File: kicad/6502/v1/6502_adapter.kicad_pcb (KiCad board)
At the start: 2 copper layers, 49 x 75.2 mm, 53 parts, among them P1 Conn_02x20_Odd_Even, P2 Conn_02x20_Odd_Even, P3 Conn_01x03, SW1 SW_Push, SW2 SW_Push, U1 WD65C02, U2 74LVC4245, U3 74LVC4245, U4 74LVC4245, U5 74LVC4245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

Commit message: Kicad 6502: final tweaks
Change-Id: Id3d45fc11b7cfa304b3275ba0561da354e969d0a
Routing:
- net /5V: track 231.6 -> 232.9 mm
- net /nML: track 35.8 -> 34.9 mm
- net /RnW: track 45.1 -> 45.6 mm
- net /GND: track 264.4 -> 264.9 mm, vias 33 -> 34
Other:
- board text added: "BkPt"
- board text added: "Optional bus enable components"
- board text removed: "BrkPt"
- board text removed: "Optional Bus Enable (BE) components"

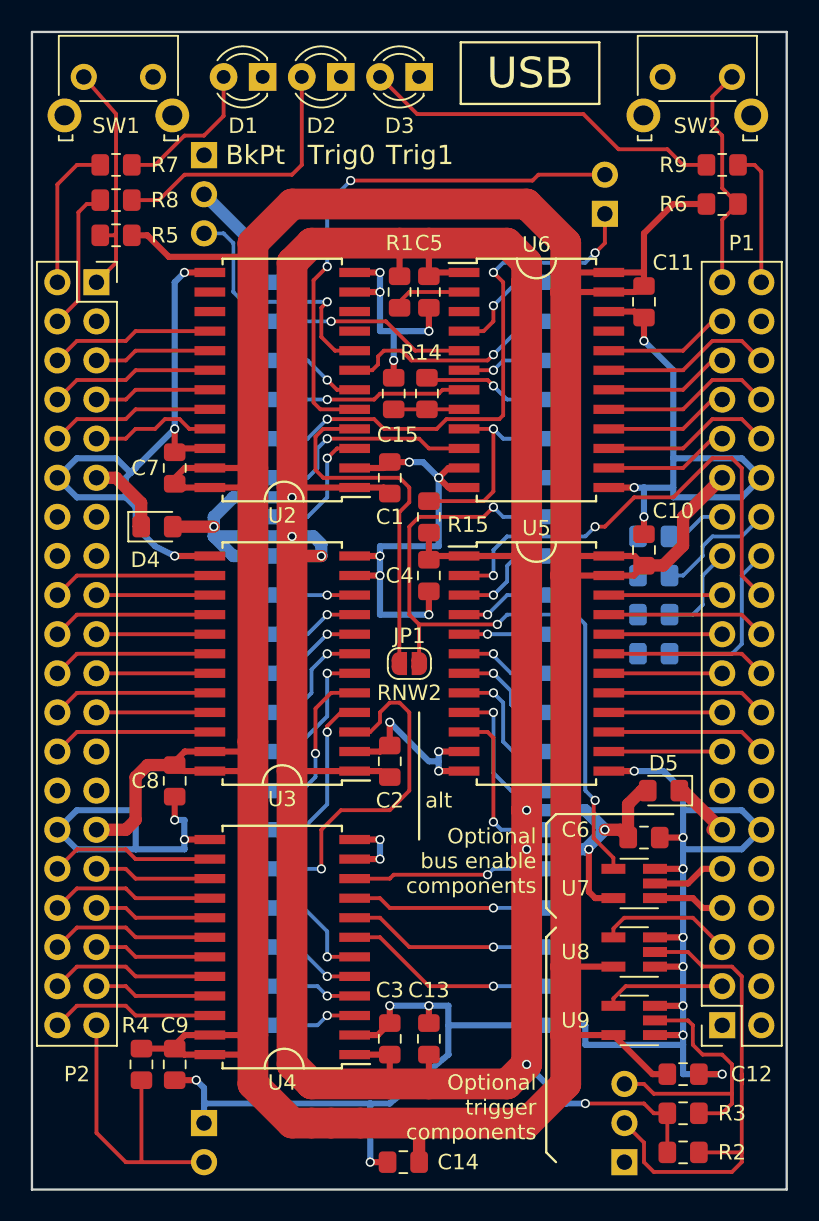
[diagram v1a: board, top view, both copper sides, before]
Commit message: Kicad 6502: add more power vias
Change-Id: I293a495840e0f96dae8bd8866a7b1adfe1f79e49
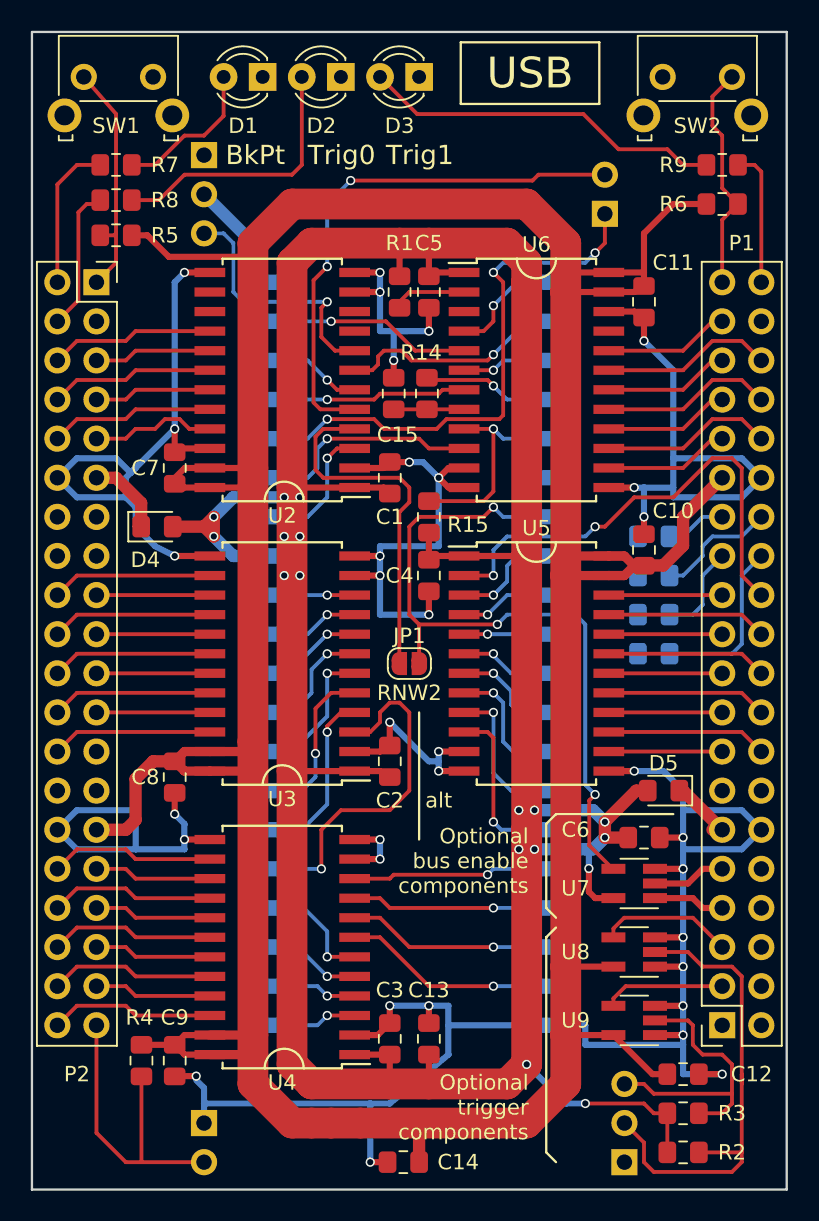
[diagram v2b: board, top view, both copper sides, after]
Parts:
- moved C9 0.25 mm to (177.8, 116.6)
- moved R4 0.25 mm to (175.6, 116.6)
- moved C8 0.24 mm to (177.8, 98.2)
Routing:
- net /5V: track 232.9 -> 234.4 mm, vias 10 -> 17
- net /3V3: track 259.0 -> 258.0 mm
- net /GND: track 264.9 -> 264.3 mm

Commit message: Kicad 6502: change via sizes
Change-Id: I8dcd3cc5ac6fae908891b67d9d1c4ddfbb9d1988
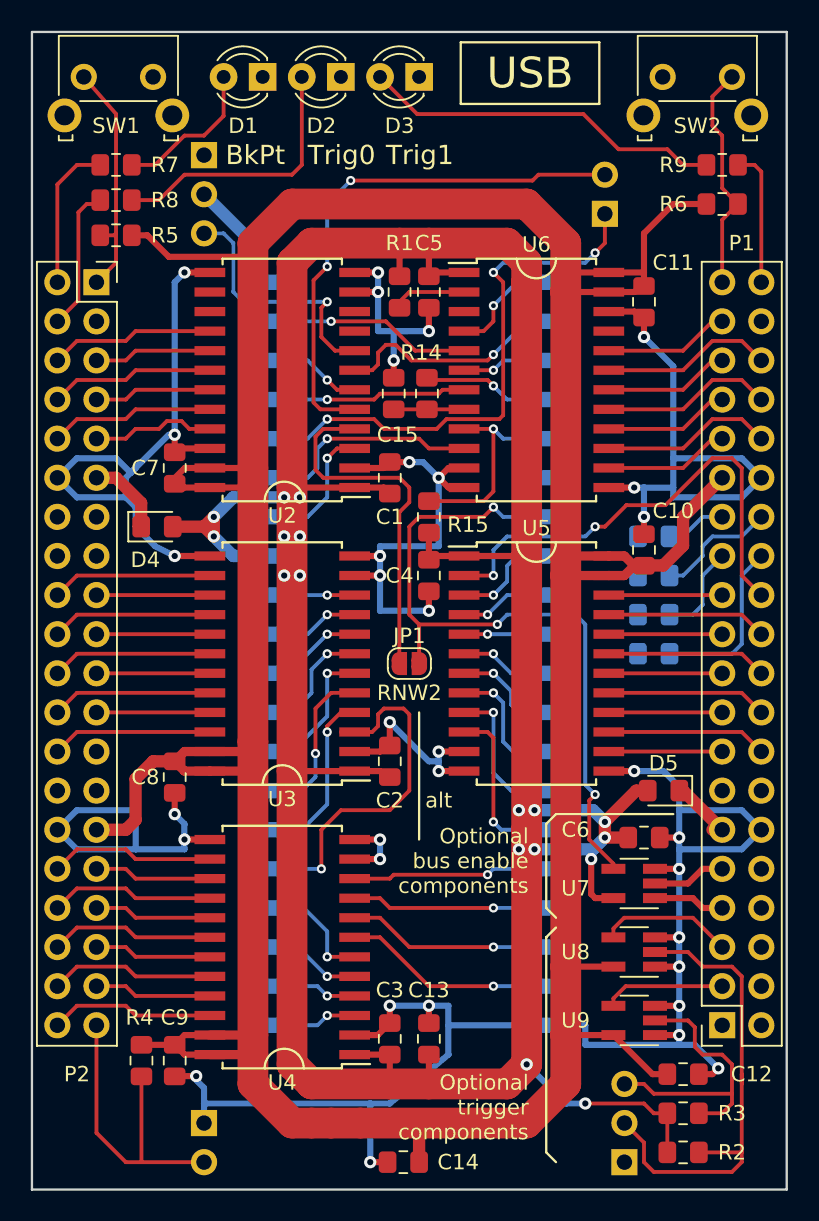
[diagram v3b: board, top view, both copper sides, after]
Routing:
- net /GND: track 264.3 -> 260.8 mm
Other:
- net class Default: via_drill 0.4 -> 0.3
- net class Power: via_dia 0.6 -> 0.8
- rule via_min_size: 0.4 -> 0.6

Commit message: kicad 6502: added weak pullups to 6502 control signals
Change-Id: Iba7afce3f12305b795a8ec8d95fa880e29d4dc03
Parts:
- added R16: 22K, Resistor_SMD:R_0805_2012Metric_Pad1.15x1.40mm_HandSolder, B.Cu at (206.5, 71.1)
- added R17: 22K, Resistor_SMD:R_0805_2012Metric_Pad1.15x1.40mm_HandSolder, B.Cu at (206.5, 68.6)
- added R18: 22K, Resistor_SMD:R_0805_2012Metric_Pad1.15x1.40mm_HandSolder, B.Cu at (179.6, 68.6)
- added R19: 22K, Resistor_SMD:R_0805_2012Metric_Pad1.15x1.40mm_HandSolder, B.Cu at (179.6, 71.1)
- added R20: 22K, Resistor_SMD:R_0805_2012Metric_Pad1.15x1.40mm_HandSolder, B.Cu at (179.6, 73.7)
- D4, D5: value MBR130 -> PMEG3010BEA; footprint Diode_SMD:D_0805_2012Metric_Pad1.15x1.40mm_HandSolder -> Diode_SMD:D_SOD-323_HandSoldering
- R15: moved to B.Cu
- moved R15 14.4 mm to (206.5, 73.7), turned to 180 degrees
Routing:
- net /5V: track 234.3 -> 256.0 mm, vias 17 -> 19
- net /nNMI: track 13.2 -> 22.2 mm
- net /nRST: track 5.98 -> 12.6 mm
- net /nIRQ: track 11.4 -> 17.3 mm
- net /nSO: track 4.33 -> 9.15 mm
- net /RDY: track 12.0 -> 16.8 mm
- net /BE: track 12.8 -> 11.0 mm
- net /GND: track 260.8 -> 259.5 mm
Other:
- board text added: "ICE-65C02 In-Circuit Emulator © 2019 Hoglet - Version 1.10"
- board text removed: "ICE-65C02 In-Circuit Emulator © 2019 Hoglet - Version 1.00"
